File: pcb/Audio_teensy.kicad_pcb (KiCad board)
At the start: 2 copper layers, 47.2 x 44.5 mm, 20 parts, among them J1 0855025008, J2 SSM-114-L-SV-BE, J3 SSM-114-L-SV-BE, J4 MJ-3523-SMT, J5 MJ-3523-SMT, U1 Teensy 3.2, U2 AP7313, U3 SGTL5000

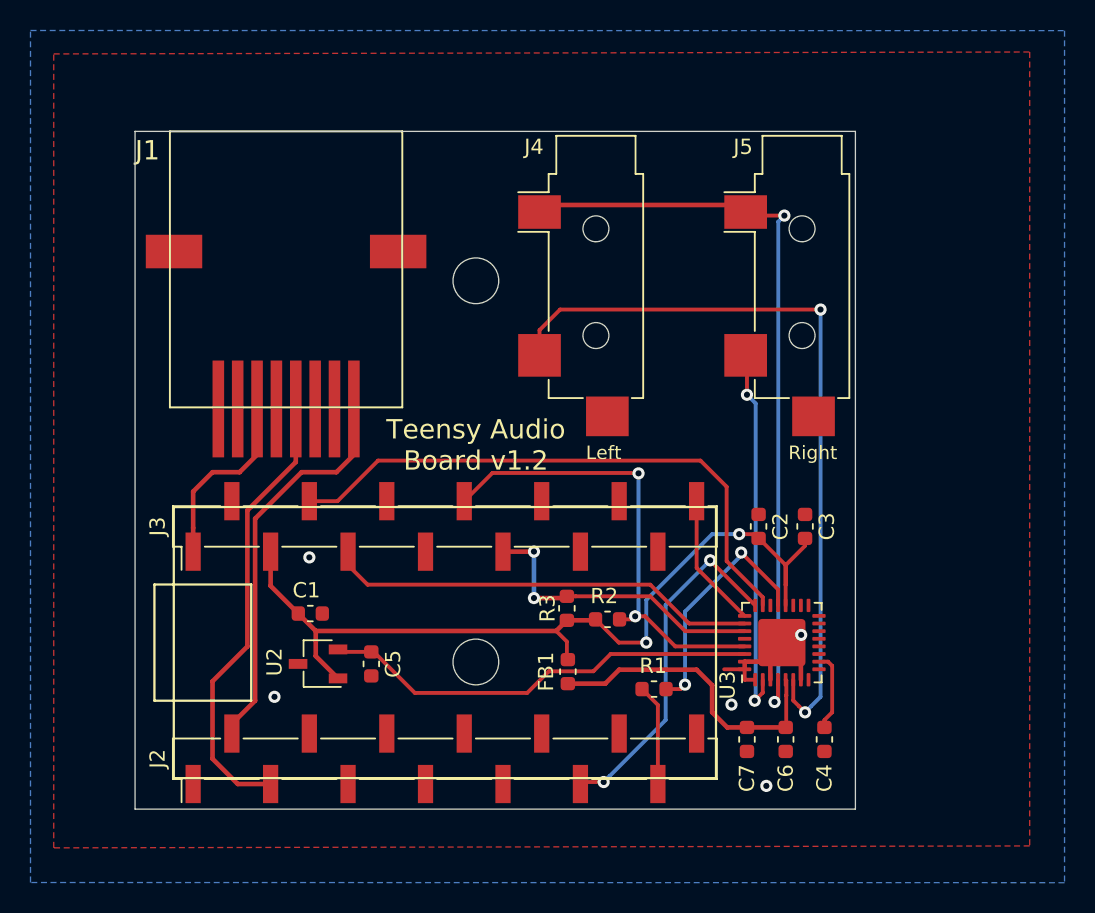
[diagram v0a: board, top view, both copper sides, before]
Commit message: changed to through hole components
rearranged mono jacks to point towards opposite sides
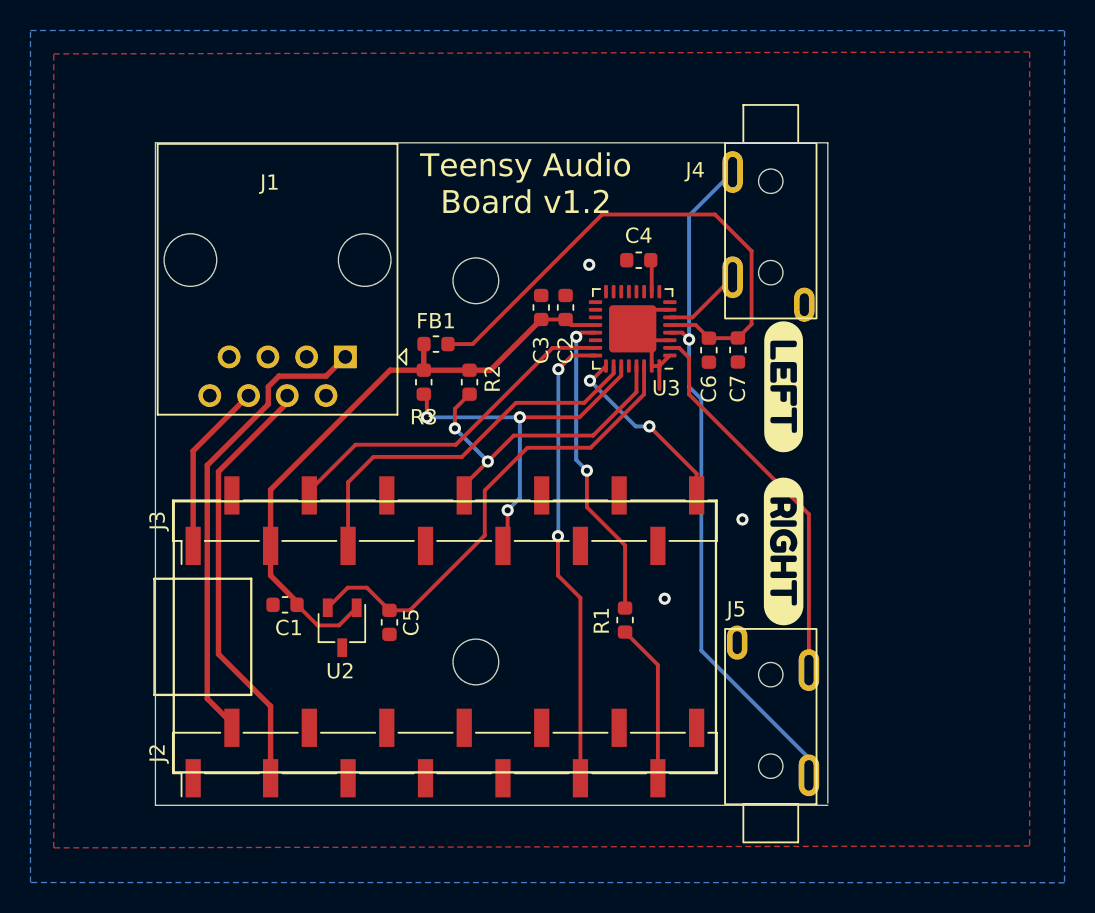
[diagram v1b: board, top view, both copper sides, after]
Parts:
- added svg2mod: G***, svg2mod, F.Cu at (160.9, 110.1)
- added svg2mod: G***, svg2mod, F.Cu at (160.9, 99.3)
- J1: footprint asl_footprints:RJ45_SMD -> asl_footprints:RJ45_THP_Vertical
- J4, J5: value MJ-3523-SMT -> 4832.2230; footprint asl_footprints:MonoJack -> asl_footprints:mono_jack_throughhole
- moved C4 33.7 mm to (151.4, 91.0), turned to 180 degrees
- moved J5 33.4 mm to (160.1, 124.8), turned to 180 degrees
- moved C6 26.0 mm to (156.0, 96.9)
- moved C7 25.5 mm to (157.9, 96.9)
- moved FB1 23.2 mm to (138.1, 96.5), turned to 180 degrees
- moved U3 22.8 mm to (151.0, 95.5), turned to 180 degrees
- moved C3 22.5 mm to (145.0, 94.1)
- moved C2 19.1 mm to (146.6, 94.1)
- moved R2 18.0 mm to (140.3, 99.0), turned to -90 degrees
- moved R3 17.6 mm to (137.3, 99.0), turned to -90 degrees
- moved J4 13.0 mm to (160.1, 85.2)
- moved J1 8.46 mm to (127.7, 91.0)
- moved R1 4.91 mm to (150.5, 114.6), turned to 90 degrees
- moved C5 2.97 mm to (135.1, 114.8)
- moved U2 2.86 mm to (131.9, 115.1), turned to -90 degrees
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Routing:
- net Net-(J4-PadT): track 49.9 -> 5.21 mm, vias 2 -> 0
- net Net-(U1-Pad30): track 37.9 -> 22.7 mm
- net /3.3VDC: track 55.8 -> 41.0 mm, vias 2 -> 0
- net Net-(C6-Pad2): track 20.4 -> 35.3 mm
- net Net-(R2-Pad2): track 30.8 -> 21.6 mm
- net /BCLK: track 23.2 -> 30.0 mm
- net Net-(J4-PadS): track 50.3 -> 45.2 mm, vias 2 -> 1
- net Net-(R3-Pad2): track 19.9 -> 24.7 mm, vias 2 -> 3
- net /MCLK: track 16.0 -> 20.5 mm
- net Net-(J1-Pad1): track 25.9 -> 30.3 mm
- net Net-(U1-Pad29): track 28.5 -> 24.7 mm
- net Net-(R1-Pad1): track 6.66 -> 10.2 mm
- net Net-(U1-Pad20): track 8.83 -> 12.1 mm, vias 0 -> 2
- net Net-(C4-Pad1): track 5.23 -> 2.09 mm
- net /1.8VDC: track 28.9 -> 31.4 mm
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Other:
- board size 47.2 x 44.5 mm -> 44.1 x 43.5 mm
- board text removed: "Left"
- board text removed: "Right"

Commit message: pcb v1.3
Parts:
- moved J2 39.6 mm to (160.1, 124.8), turned to 180 degrees
- moved J3 39.6 mm to (160.1, 85.2), turned to 0 degrees
- moved svg2mod 10.9 mm to (160.6, 110.2), turned to 90 degrees
- moved svg2mod 10.1 mm to (160.7, 100.0), turned to 90 degrees
- moved FB1 5.60 mm to (143.7, 96.7), turned to -90 degrees
- moved R3 1.60 mm to (148.9, 114.6)
- moved J5 1.08 mm to (137.6, 108.1)
- moved U2 1.08 mm to (137.6, 115.7)
- moved J4 1.05 mm to (137.6, 123.3)
- moved C2 0.40 mm to (147.0, 94.1)
- moved C3 0.40 mm to (145.4, 94.1)
- renumbered C6 to C4, C7 to C5, C5 to C6, C4 to C7, J4 to J2, J5 to J3, J2 to J4, J3 to J5, R3 to R1, R1 to R3, U2 to U1, U1 to U2
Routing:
- net Net-(J2-PadT): track 5.21 -> 29.5 mm, vias 0 -> 1
- net Net-(J3-PadT): track 25.0 -> 10.7 mm
- net Net-(C4-Pad2): track 35.3 -> 26.5 mm
- net Net-(U2-Pad30): track 22.7 -> 24.3 mm
- net Net-(R2-Pad2): track 21.6 -> 22.6 mm
- net /BCLK: track 30.0 -> 30.7 mm
- net Net-(U2-Pad29): track 24.7 -> 25.5 mm
- net /5VDC: track 11.1 -> 11.8 mm
- net /MCLK: track 20.5 -> 19.8 mm
- net Net-(R3-Pad1): track 10.2 -> 10.7 mm
- net GND: vias 3 -> 4
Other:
- outline, holes or cut-outs redrawn
- rule pad_to_mask_clearance: 0.0508 -> 0
- board text added: "Teensy Audio Board v1.3"
- board text removed: "Teensy Audio Board v1.2"
